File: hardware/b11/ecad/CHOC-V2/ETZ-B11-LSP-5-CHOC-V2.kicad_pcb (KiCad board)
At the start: 2 copper layers, 163.9 x 90.2 mm, 339 parts

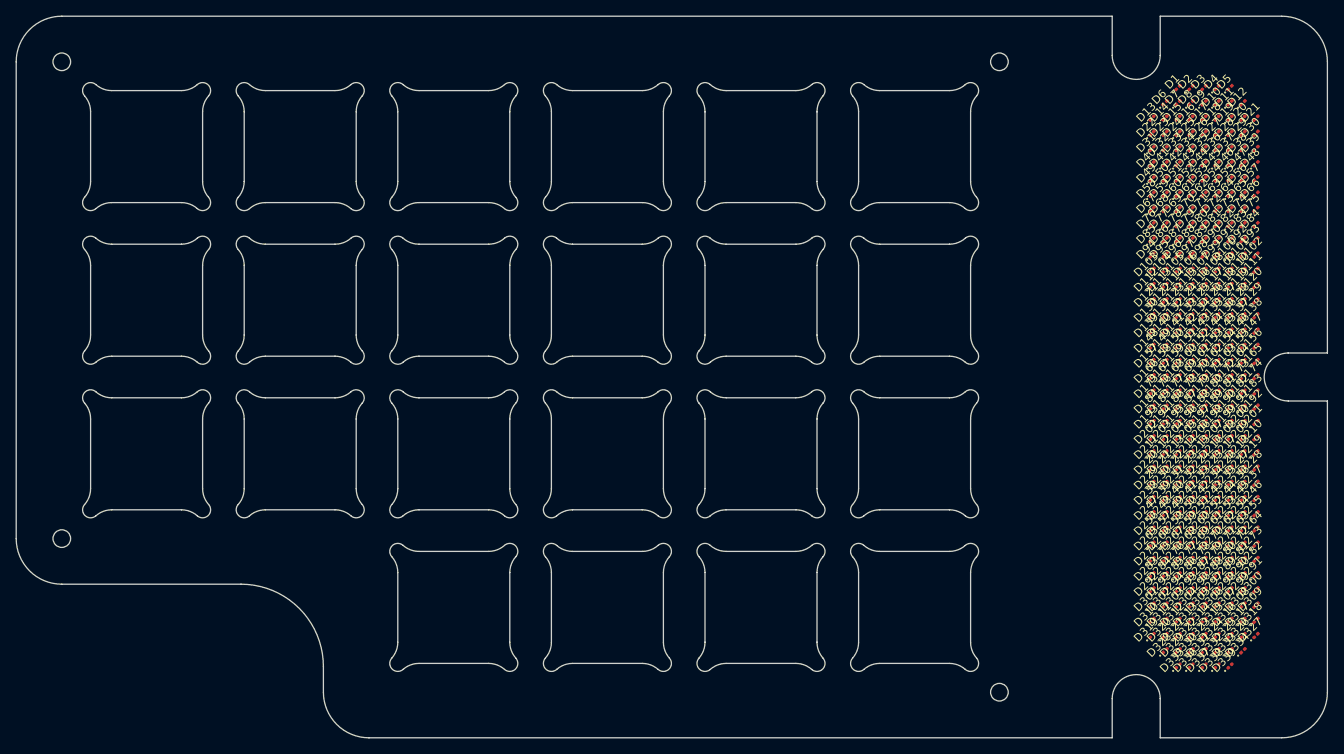
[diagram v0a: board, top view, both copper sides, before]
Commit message: refactor(hardware/b11): restructure ecad + tools, add KS-33 boards
- Rename PCB files: *-N → *-MX, *-L → *-CHOC-V2
- Reorganise ecad/ into per-family subfolders (MX/, CHOC-V2/, KS-33/)
- Add 8 blank KS-33 boards (outline only, human-populated ad-hoc)
- Apply JLCPCB-validated stackup (white/black/FR4 natural/black/white)
  to all 24 boards; SP boards at correct family thickness
- Add hardware/b11/tools/: config.py, placement.py, place-switch-sockets.py,
  place-switch-leds.py, place-display-leds.py — family-aware, non-destructive
- Archive old placement + generation scripts to hardware/scripts/_archive/
- Remove switch-origins.yaml (replaced by GRID_ORIGINS in config.py)
- Add PLAN.md tracking refactor progress

Co-Authored-By: Claude Sonnet 4.6 <noreply@anthropic.com>
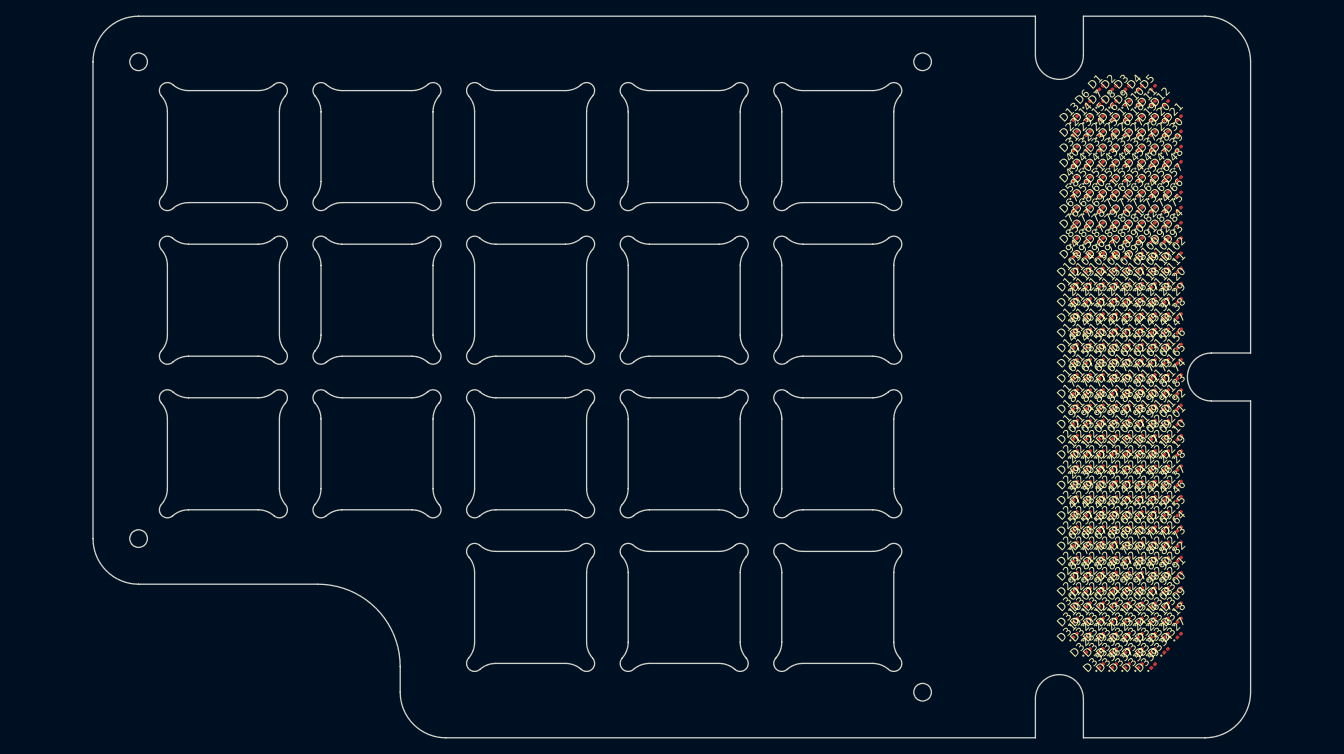
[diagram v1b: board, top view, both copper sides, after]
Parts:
- moved D1 9.60 mm to (202.2, 68.1)
- moved D10 9.60 mm to (207.1, 70.0)
- moved D100 9.60 mm to (208.7, 89.1)
- moved D101 9.60 mm to (210.3, 89.1)
- moved D102 9.60 mm to (211.9, 89.1)
- moved D103 9.60 mm to (198.9, 91.0)
- moved D104 9.60 mm to (200.6, 91.0)
- moved D105 9.60 mm to (202.2, 91.0)
- moved D106 9.60 mm to (203.8, 91.0)
- moved D107 9.60 mm to (205.4, 91.0)
- moved D108 9.60 mm to (207.1, 91.0)
- moved D109 9.60 mm to (208.7, 91.0)
- moved D11 9.60 mm to (208.7, 70.0)
- moved D110 9.60 mm to (210.3, 91.0)
- moved D111 9.60 mm to (211.9, 91.0)
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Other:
- board size 163.9 x 90.2 mm -> 144.7 x 90.2 mm
